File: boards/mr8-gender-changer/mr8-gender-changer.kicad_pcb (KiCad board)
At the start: 2 copper layers, 14.6 x 28 mm, 9 parts, among them J1 Conn_02x05_Odd_Even, J2 Conn_01x02, J3 Conn_01x08

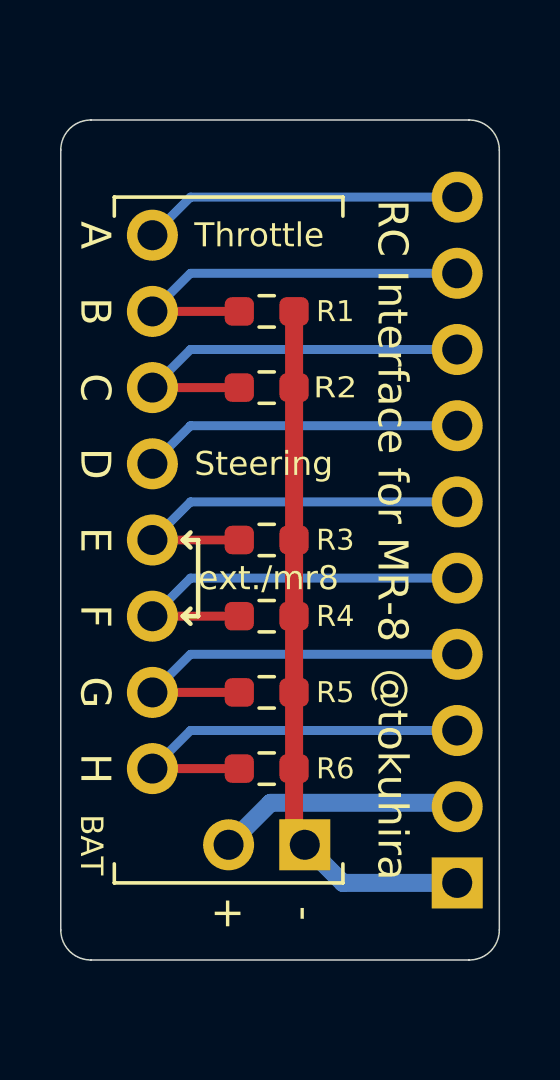
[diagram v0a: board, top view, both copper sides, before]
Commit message: KiCad 7
Update file names and formats for KiCad 7.
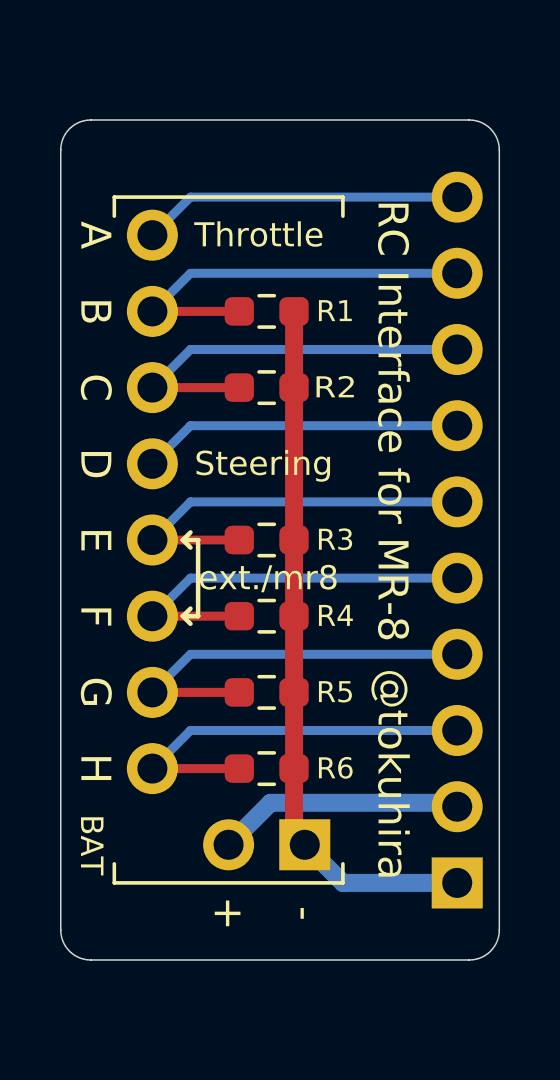
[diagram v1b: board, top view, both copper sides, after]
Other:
- net class Default removed
- net class Power removed
